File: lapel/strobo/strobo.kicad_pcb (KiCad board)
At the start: 2 copper layers, 50 x 50 mm, 31 parts, among them J1 USB_C_Receptacle_PowerOnly_6P, U1 ICM7556, U2 MCP73831-2-MC

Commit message: feat(strobo): route PCB, reposition U1, update design rules
- Add track segments (GND, CC1, power nets)
- Move U1 (SOIC-14) to 50,58.5
- Set min clearance 0.1mm, add track width 1.0mm, via 1.0/0.5mm
- Add diff pair dims entry
- Clear component Description fields
- Remove freerouting.dsn temp files
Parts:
- R2: footprint Capacitor_SMD:C_0805_2012Metric_Pad1.18x1.45mm_HandSolder -> Resistor_SMD:R_0805_2012Metric_Pad1.20x1.40mm_HandSolder
- moved R1 33.5 mm to (56.5, 68.0), turned to -90 degrees
- moved R2 16.8 mm to (58.5, 68.0), turned to -90 degrees
- moved U1 13.2 mm to (50.0, 58.5)
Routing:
- net Net-(J1-CC1): track 0.00 -> 14.6 mm
- net Net-(J1-CC2): track 0.00 -> 9.01 mm
- net GND: track 0.00 -> 8.37 mm

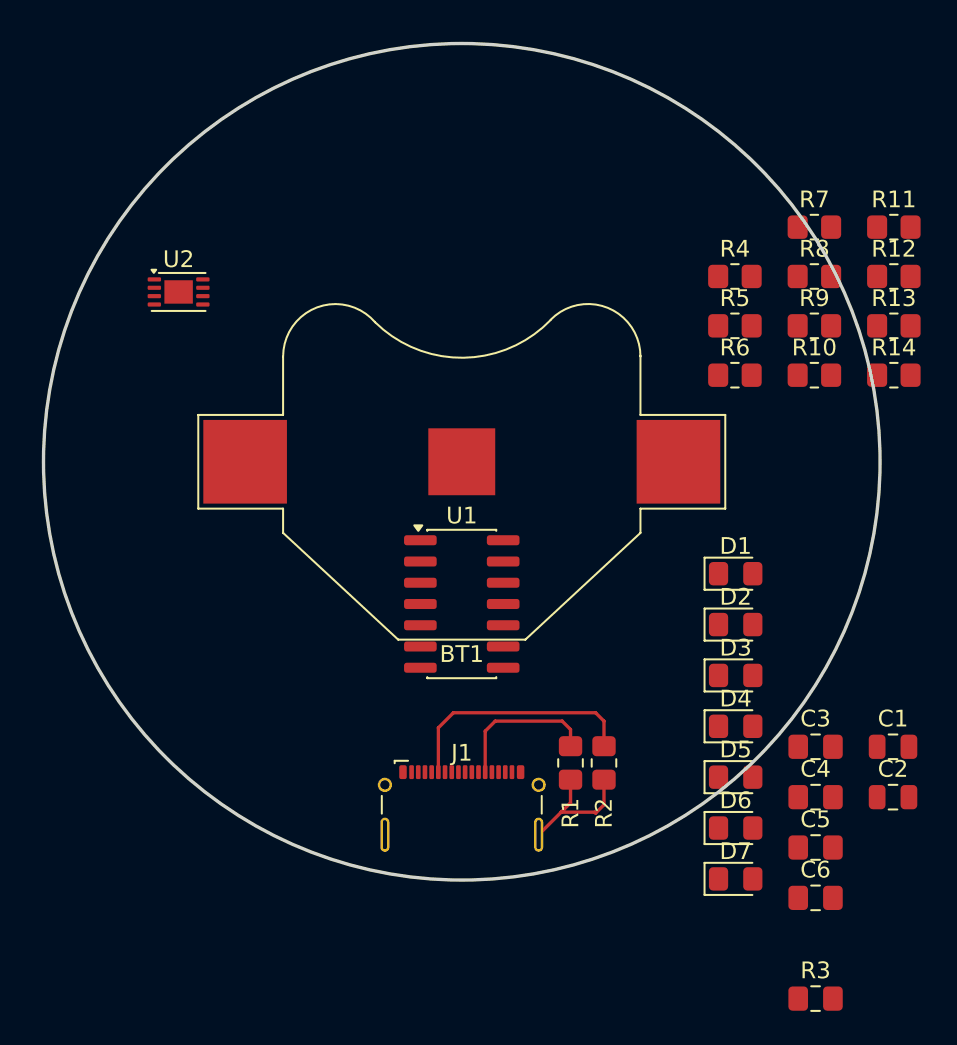
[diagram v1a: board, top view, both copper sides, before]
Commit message: feat(strobo): PCB layout, schematic updates, and fabrication outputs
- Add SW_SPDT symbol to schematic
- Major PCB layout rework (routing, component placement)
- Add DRC exclusions with justification notes
- Configure ngspice simulation workbook
- Set plot output path to dist/
- Change dimension units to mm
- Add ICM7556 custom component library
- Add freerouting session file and round-tracks config
- Add fabrication outputs: gerbers, drill files, BOM, iBOM, zip
- Add kit.yml project config
- Add .pi/gsd agent config and workflows
- Update .gitignore: ignore lock files, .history/, temp-freerouting.dsn
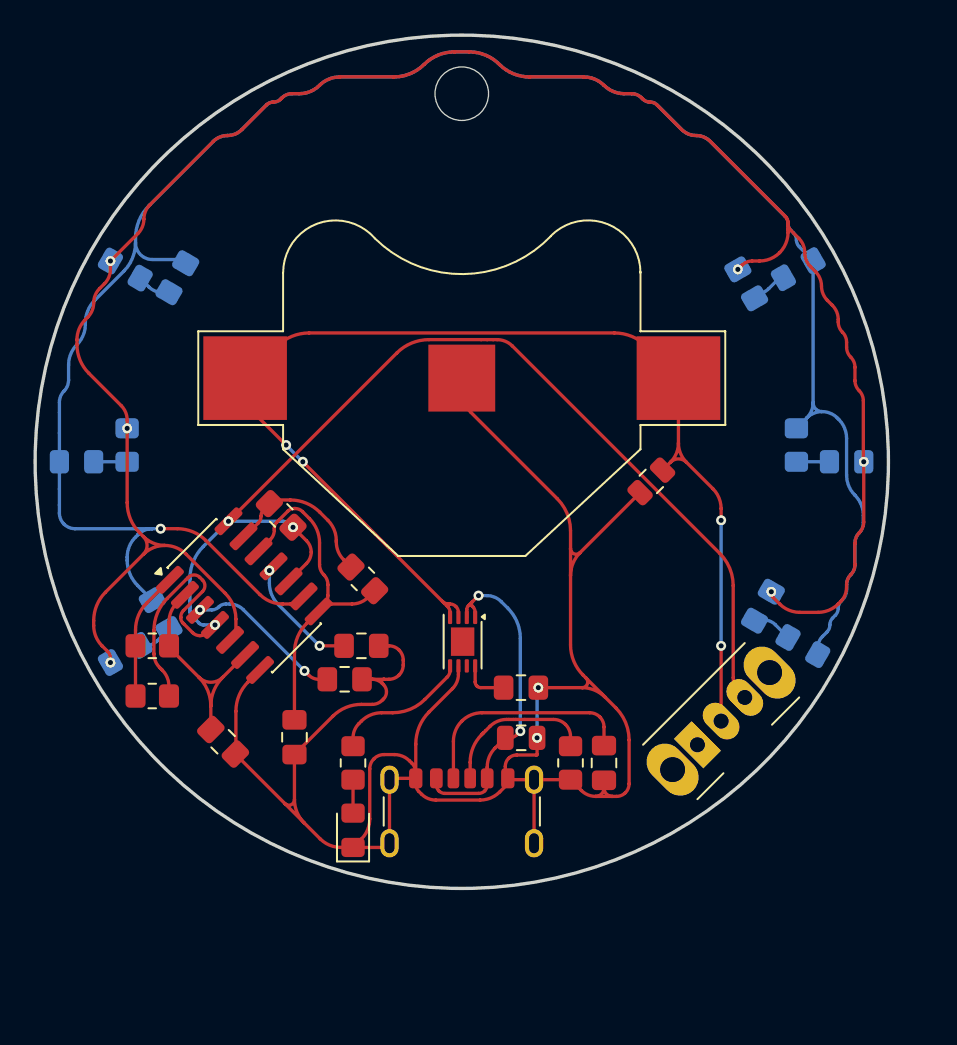
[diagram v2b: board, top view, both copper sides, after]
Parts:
- added Image: , LOGO, B.Cu at (50.0, 49.0)
- added REF**: MountingHole_3.2mm_M3_DIN965, MountingHole:MountingHole_3.2mm_M3_DIN965, F.Cu at (50.0, 28.0)
- added SW1: SW_SPDT, Button_Switch_THT:SW_Slide_SPDT_Angled_CK_OS102011MA1Q, F.Cu at (64.1, 66.9)
- D2, D3, D4, D5, D6, D7, R10, R11, R12, R13, R14, R9: moved to B.Cu
- J1: footprint Connector_USB:USB_C_Receptacle_G-Switch_GT-USB-7025 -> Connector_USB:USB_C_Receptacle_GCT_USB4125-xx-x-0190_6P_TopMnt_Horizontal
- R2: footprint Resistor_SMD:R_0805_2012Metric_Pad1.20x1.40mm_HandSolder -> Capacitor_SMD:C_0805_2012Metric_Pad1.18x1.45mm_HandSolder
- moved D7 51.5 mm to (29.9, 38.5), turned to -30 degrees
- moved R11 47.6 mm to (30.0, 49.0), turned to 90 degrees
- moved R13 47.1 mm to (32.0, 59.1), turned to 120 degrees
- moved R14 43.2 mm to (33.0, 39.0), turned to 60 degrees
- moved D4 42.4 mm to (27.0, 50.0)
- moved R5 41.3 mm to (31.5, 64.0), turned to 180 degrees
- moved R6 38.4 mm to (31.5, 61.0)
- moved D6 37.9 mm to (29.9, 61.5), turned to 30 degrees
- moved R4 37.0 mm to (43.5, 68.0), turned to -90 degrees
- moved R7 36.2 mm to (39.2, 53.2), turned to 135 degrees
- moved C3 35.4 mm to (35.7, 66.7), turned to -45 degrees
- moved R8 32.5 mm to (44.1, 57.0), turned to -45 degrees
- moved C5 31.8 mm to (40.0, 66.5), turned to -90 degrees
- moved C6 31.0 mm to (44.0, 61.0), turned to 180 degrees
- moved C4 29.0 mm to (43.0, 63.0), turned to 180 degrees
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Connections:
- BT1 pad 1: +3.3V -> Net-(BT1-+)
- C2 pad 1: +3.3V -> Net-(BT1-+)
- U2 pad 3: +3.3V -> Net-(BT1-+)
- U2 pad 4: +3.3V -> Net-(BT1-+)
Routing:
- net Net-(D2-K): track 0.00 -> 121.2 mm, vias 0 -> 1
- net Net-(D3-K): track 0.00 -> 120.8 mm, vias 0 -> 6
- net GND: track 8.37 -> 121.0 mm, vias 0 -> 2
- net +3.3V: track 0.00 -> 77.2 mm, vias 0 -> 3
- net Net-(BT1-+): track 0.00 -> 65.0 mm, vias 0 -> 4
- net Net-(U1B-THRES): track 0.00 -> 19.3 mm
- net Net-(C1-Pad1): track 0.00 -> 18.6 mm, vias 0 -> 2
- net Net-(U1A-THRES): track 0.00 -> 13.9 mm
- net Net-(U1A-CONT): track 0.00 -> 9.47 mm, vias 0 -> 2
- net Net-(U1B-DISCH): track 0.00 -> 8.72 mm
- net Net-(U1A-DISCH): track 0.00 -> 7.69 mm
- net Net-(U2-STAT): track 0.00 -> 7.62 mm
- net Net-(U1B-CONT): track 0.00 -> 7.12 mm, vias 0 -> 2
- net Net-(U2-PROG): track 0.00 -> 2.85 mm
- net Net-(D4-A): track 0.00 -> 2.00 mm
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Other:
- board size 50 x 50 mm -> 51 x 51 mm
